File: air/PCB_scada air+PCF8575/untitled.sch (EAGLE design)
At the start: 122 parts, among them J1 C-GRID-03-70543, J10 C-GRID-03-70543, J11 C-GRID-03-70543, J12 C-GRID-03-70543, J13 C-GRID-03-70543, J14 C-GRID-03-70543, J15 C-GRID-03-70543, J16 C-GRID-03-70543, J17 C-GRID-03-70543, J18 C-GRID-03-70543, J19 C-GRID-03-70543, J2 C-GRID-03-70543, J20 C-GRID-03-70543, J21 C-GRID-03-70543, J3 C-GRID-03-70543, J4 C-GRID-03-70543, J5 C-GRID-03-70543, J6 C-GRID-03-70543, J7 C-GRID-03-70543, J8 C-GRID-03-70543, J9 C-GRID-03-70543, K1 351, Q1 MMBT2222, Q10 MMBT2222, Q11 MMBT2222, Q12 MMBT2222, Q13 MMBT2222, Q14 MMBT2222, Q15 MMBT2222, Q16 MMBT2222, Q17 MMBT2222, Q18 MMBT2222, Q19 MMBT2222, Q2 MMBT2222, Q20 MMBT2222, Q21 MMBT2222, Q22 S9013, Q3 MMBT2222, Q4 MMBT2222, Q5 MMBT2222, Q6 MMBT2222, Q7 MMBT2222, Q8 MMBT2222, Q9 MMBT2222, U1 ESP32-DEVKITC-32D, U2 PCF8575PW, U3 PCF8575PW, U4 PC817X2NIP0F, X1 C-GRID-02-70543, X2 C-GRID-02-70543, X3 MSTBA2, X4 C-GRID-03-70543, X5 C-GRID-02-70543, X6 C-GRID-02-70543, X7 MSTBA2, X8 MSTBA4, X9 MSTBA2

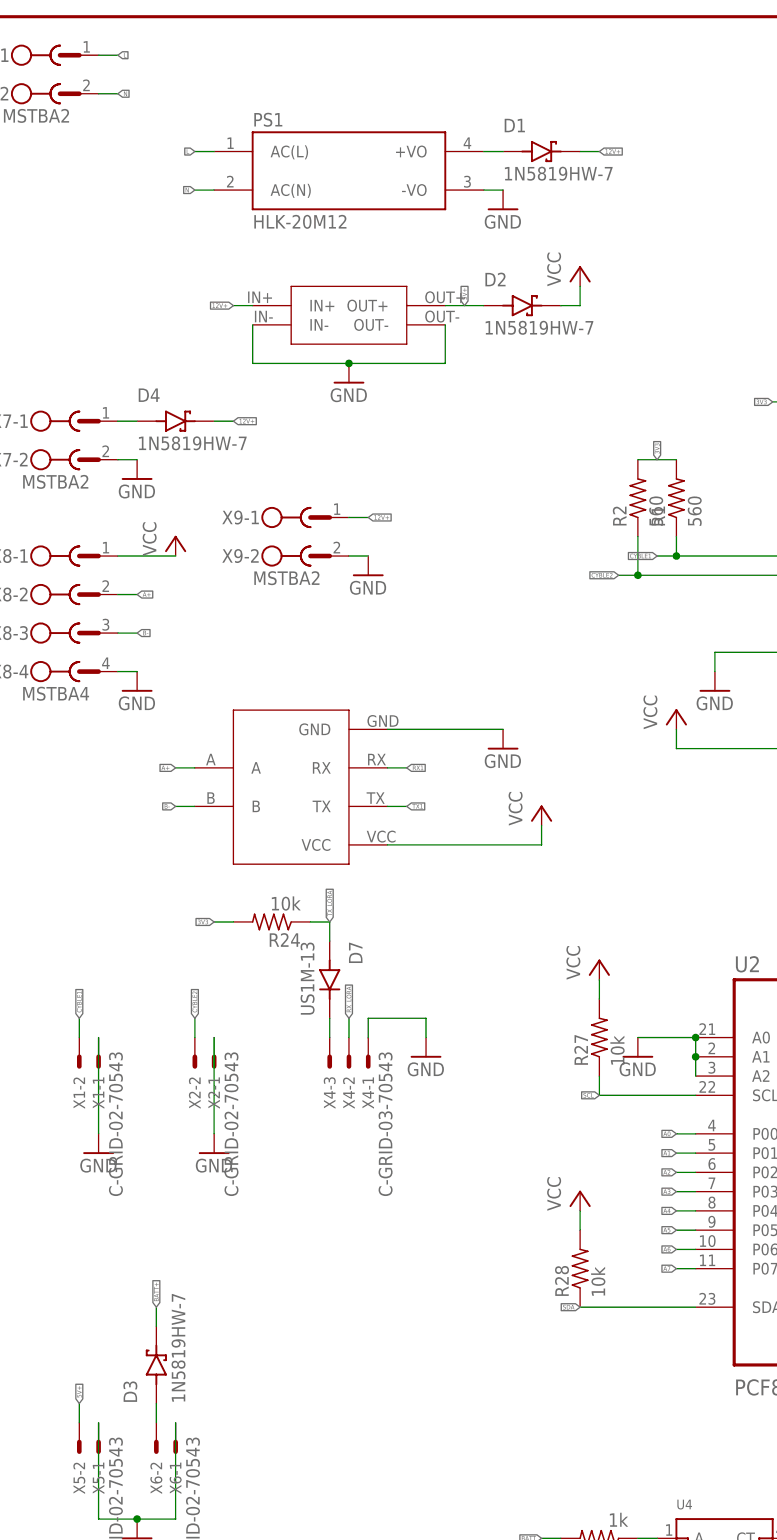
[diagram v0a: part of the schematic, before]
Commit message: revisi dioda schotky
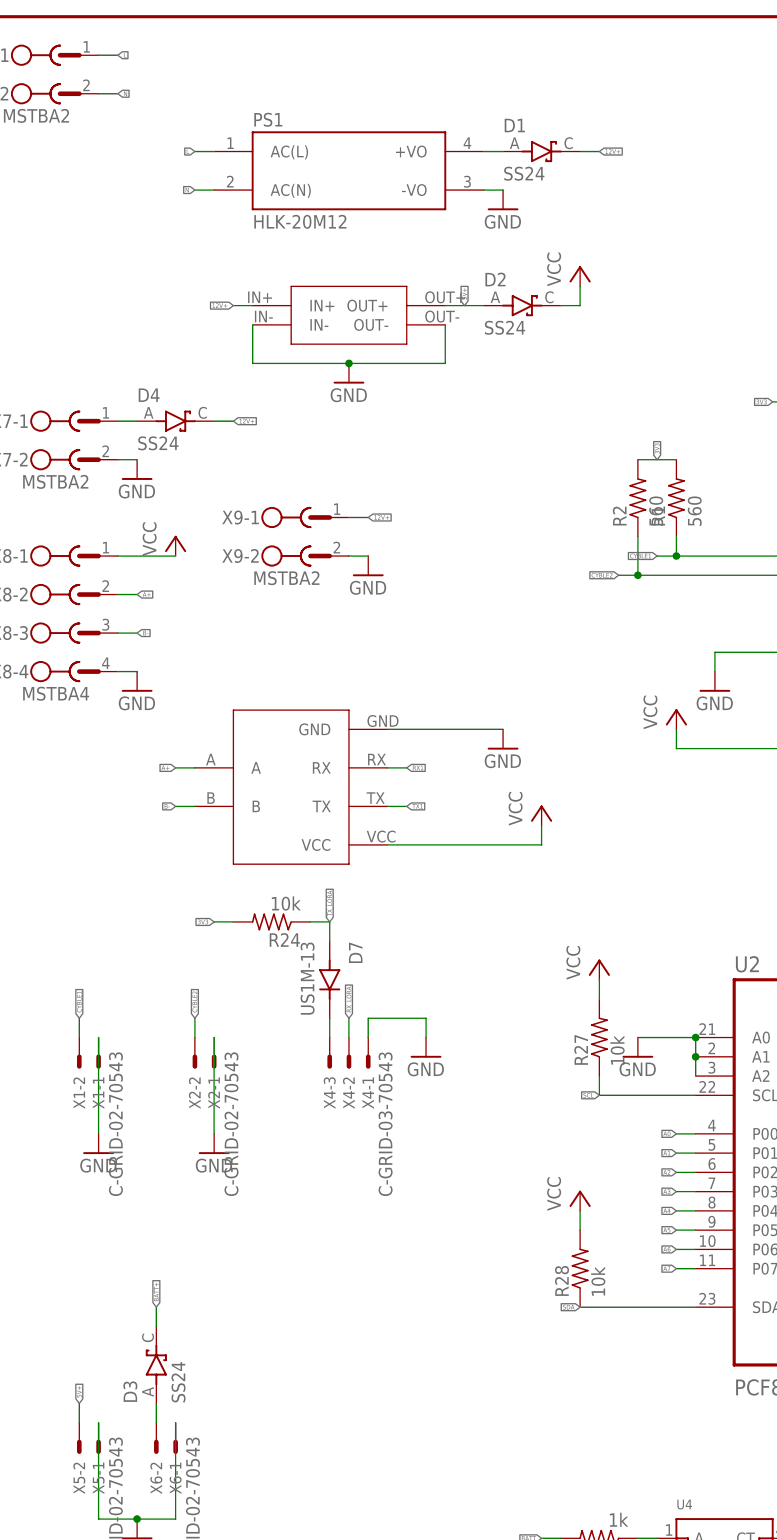
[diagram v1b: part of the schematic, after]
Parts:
- D1, D2, D3, D4: value 1N5819HW-7 -> SS24; device 1N5819HW-7:1N5819HW-7 -> SS24:SS24
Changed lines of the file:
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@@
 <part name="PS1" library="HLK-20M12" deviceset="HLK-20M12" device=""/>
 <part name="GND12" library="supply1" library_urn="urn:adsk.eagle:library:371" deviceset="GND" device=""/>
-<part name="D1" library="1N5819HW-7" deviceset="1N5819HW-7" device=""/>
+<part name="D1" library="SS24" deviceset="SS24" device=""/>
 <part name="MINI1" library="MINI560" deviceset="MINI560" device=""/>
 <part name="GND13" library="supply1" library_urn="urn:adsk.eagle:library:371" deviceset="GND" device=""/>
@@
 <part name="X4" library="con-molex" library_urn="urn:adsk.eagle:library:165" deviceset="C-GRID-03" device="-70543" package3d_urn="urn:adsk.eagle:package:8078684/1"/>
 <part name="GND20" library="supply1" library_urn="urn:adsk.eagle:library:371" deviceset="GND" device=""/>
-<part name="D2" library="1N5819HW-7" deviceset="1N5819HW-7" device=""/>
+<part name="D2" library="SS24" deviceset="SS24" device=""/>
 <part name="P+3" library="supply1" library_urn="urn:adsk.eagle:library:371" deviceset="VCC" device=""/>
 <part name="X5" library="con-molex" library_urn="urn:adsk.eagle:library:165" deviceset="C-GRID-02" device="-70543" package3d_urn="urn:adsk.eagle:package:8078681/1"/>
 <part name="X6" library="con-molex" library_urn="urn:adsk.eagle:library:165" deviceset="C-GRID-02" device="-70543" package3d_urn="urn:adsk.eagle:package:8078681/1"/>
 <part name="GND21" library="supply1" library_urn="urn:adsk.eagle:library:371" deviceset="GND" device=""/>
-<part name="D3" library="1N5819HW-7" deviceset="1N5819HW-7" device=""/>
+<part name="D3" library="SS24" deviceset="SS24" device=""/>
 <part name="Q1" library="MMBT2222_" deviceset="MMBT2222*" device=""/>
 <part name="Q2" library="MMBT2222_" deviceset="MMBT2222*" device=""/>
@@
 <part name="P+7" library="supply1" library_urn="urn:adsk.eagle:library:371" deviceset="VCC" device=""/>
 <part name="X7" library="con-phoenix-508" library_urn="urn:adsk.eagle:library:176" deviceset="MSTBA2" device="" package3d_urn="urn:adsk.eagle:package:9615/1"/>
-<part name="D4" library="1N5819HW-7" deviceset="1N5819HW-7" device=""/>
+<part name="D4" library="SS24" deviceset="SS24" device=""/>
 <part name="GND22" library="supply1" library_urn="urn:adsk.eagle:library:371" deviceset="GND" device=""/>
 <part name="TTL-RS1" library="TTL-RS485" deviceset="TTL-RS485" device=""/>

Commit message: revisi scada air
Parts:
- added JP1, JP2: (no value), adafruit:PINHD-1X3CB
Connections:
- new net GND1: JP1.1, JP1.2, JP1.3, JP2.1, JP2.2, JP2.3
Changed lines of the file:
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@@
 <layer number="48" name="Document" color="7" fill="1" visible="no" active="no"/>
 <layer number="49" name="Reference" color="7" fill="1" visible="no" active="no"/>
+<layer number="50" name="dxf" color="7" fill="1" visible="no" active="no"/>
 <layer number="51" name="tDocu" color="7" fill="1" visible="no" active="no"/>
 <layer number="52" name="bDocu" color="7" fill="1" visible="no" active="no"/>
+<layer number="53" name="tGND_GNDA" color="7" fill="9" visible="no" active="no"/>
+<layer number="54" name="bGND_GNDA" color="1" fill="9" visible="no" active="no"/>
+<layer number="56" name="wert" color="7" fill="1" visible="no" active="no"/>
+<layer number="57" name="tCAD" color="7" fill="1" visible="no" active="no"/>
+<layer number="59" name="tCarbon" color="7" fill="1" visible="no" active="no"/>
+<layer number="60" name="bCarbon" color="7" fill="1" visible="no" active="no"/>
 <layer number="88" name="SimResults" color="9" fill="1" visible="yes" active="yes"/>
 <layer number="89" name="SimProbes" color="9" fill="1" visible="yes" active="yes"/>
@@
 <layer number="97" name="Info" color="7" fill="1" visible="yes" active="yes"/>
 <layer number="98" name="Guide" color="6" fill="1" visible="yes" active="yes"/>
+<layer number="99" name="SpiceOrder" color="7" fill="1" visible="no" active="no"/>
+<layer number="100" name="Muster" color="7" fill="1" visible="no" active="no"/>
+<layer number="101" name="Patch_Top" color="12" fill="4" visible="no" active="yes"/>
+<layer number="102" name="Vscore" color="7" fill="1" visible="no" active="yes"/>
+<layer number="103" name="fp3" color="7" fill="1" visible="no" active="yes"/>
+<layer number="104" name="Name" color="7" fill="1" visible="no" active="yes"/>
+<layer number="105" name="Beschreib" color="9" fill="1" visible="no" active="yes"/>
+<layer number="106" name="BGA-Top" color="4" fill="1" visible="no" active="yes"/>
+<layer number="107" name="BD-Top" color="5" fill="1" visible="no" active="yes"/>
+<layer number="108" name="fp8" color="7" fill="1" visible="no" active="yes"/>
+<layer number="109" name="fp9" color="7" fill="1" visible="no" active="yes"/>
+<layer number="110" name="fp0" color="7" fill="1" visible="no" active="yes"/>
+<layer number="111" name="LPC17xx" color="7" fill="1" visible="no" active="yes"/>
+<layer number="112" name="tSilk" color="7" fill="1" visible="no" active="yes"/>
+<layer number="113" name="ReferenceLS" color="7" fill="1" visible="no" active="no"/>
+<layer number="116" name="Patch_BOT" color="9" fill="4" visible="no" active="yes"/>
+<layer number="118" name="Rect_Pads" color="7" fill="1" visible="no" active="no"/>
+<layer number="121" name="_tsilk" color="7" fill="1" visible="no" active="yes"/>
+<layer number="122" name="_bsilk" color="7" fill="1" visible="no" active="yes"/>
+<layer number="123" name="tTestmark" color="7" fill="1" visible="no" active="yes"/>
+<layer number="124" name="bTestmark" color="7" fill="1" visible="no" active="yes"/>
+<layer number="125" name="_tNames" color="7" fill="1" visible="no" active="yes"/>
+<layer number="126" name="_bNames" color="7" fill="1" visible="no" active="yes"/>
+<layer number="127" name="_tValues" color="7" fill="1" visible="no" active="yes"/>
+<layer number="128" name="_bValues" color="7" fill="1" visible="no" active="yes"/>
+<layer number="129" name="Mask" color="7" fill="1" visible="yes" active="yes"/>
+<layer number="131" name="tAdjust" color="7" fill="1" visible="no" active="yes"/>
+<layer number="132" name="bAdjust" color="7" fill="1" visible="no" active="yes"/>
+<layer number="144" name="Drill_legend" color="7" fill="1" visible="no" active="yes"/>
+<layer number="150" name="Notes" color="7" fill="1" visible="no" active="yes"/>
+<layer number="151" name="HeatSink" color="7" fill="1" visible="no" active="yes"/>
+<layer number="152" name="_bDocu" color="7" fill="1" visible="no" active="yes"/>
+<layer number="153" name="FabDoc1" color="6" fill="1" visible="no" active="no"/>
+<layer number="154" name="FabDoc2" color="2" fill="1" visible="no" active="no"/>
+<layer number="155" name="FabDoc3" color="7" fill="15" visible="no" active="no"/>
+<layer number="199" name="Contour" color="7" fill="1" visible="no" active="yes"/>
+<layer number="200" name="200bmp" color="1" fill="10" visible="no" active="yes"/>
+<layer number="201" name="201bmp" color="2" fill="1" visible="no" active="no"/>
+<layer number="202" name="202bmp" color="3" fill="1" visible="no" active="no"/>
+<layer number="203" name="203bmp" color="4" fill="10" visible="no" active="yes"/>
+<layer number="204" name="204bmp" color="5" fill="10" visible="no" active="yes"/>
+<layer number="205" name="205bmp" color="6" fill="10" visible="no" active="yes"/>
+<layer number="206" name="206bmp" color="7" fill="10" visible="no" active="yes"/>
+<layer number="207" name="207bmp" color="8" fill="10" visible="no" active="yes"/>
+<layer number="208" name="208bmp" color="9" fill="10" visible="no" active="yes"/>
+<layer number="209" name="209bmp" color="7" fill="1" visible="no" active="yes"/>
+<layer number="210" name="210bmp" color="7" fill="1" visible="no" active="yes"/>
+<layer number="211" name="211bmp" color="7" fill="1" visible="no" active="yes"/>
+<layer number="212" name="212bmp" color="7" fill="1" visible="no" active="yes"/>
+<layer number="213" name="213bmp" color="7" fill="1" visible="no" active="yes"/>
+<layer number="214" name="214bmp" color="7" fill="1" visible="no" active="yes"/>
+<layer number="215" name="215bmp" color="7" fill="1" visible="no" active="yes"/>
+<layer number="216" name="216bmp" color="7" fill="1" visible="no" active="yes"/>
+<layer number="217" name="217bmp" color="18" fill="1" visible="no" active="no"/>
+<layer number="218" name="218bmp" color="19" fill="1" visible="no" active="no"/>
+<layer number="219" name="219bmp" color="20" fill="1" visible="no" active="no"/>
+<layer number="220" name="220bmp" color="21" fill="1" visible="no" active="no"/>
+<layer number="221" name="221bmp" color="22" fill="1" visible="no" active="no"/>
+<layer number="222" name="222bmp" color="23" fill="1" visible="no" active="no"/>
+<layer number="223" name="223bmp" color="24" fill="1" visible="no" active="no"/>
+<layer number="224" name="224bmp" color="25" fill="1" visible="no" active="no"/>
+<layer number="225" name="225bmp" color="7" fill="1" visible="yes" active="yes"/>
+<layer number="226" name="226bmp" color="7" fill="1" visible="yes" active="yes"/>
+<layer number="227" name="227bmp" color="7" fill="1" visible="yes" active="yes"/>
+<layer number="228" name="228bmp" color="7" fill="1" visible="yes" active="yes"/>
+<layer number="229" name="229bmp" color="7" fill="1" visible="yes" active="yes"/>
+<layer number="230" name="230bmp" color="7" fill="1" visible="yes" active="yes"/>
+<layer number="231" name="Eagle3D_PG1" color="7" fill="1" visible="no" active="no"/>
+<layer number="232" name="Eagle3D_PG2" color="7" fill="1" visible="no" active="no"/>
+<layer number="233" name="Eagle3D_PG3" color="7" fill="1" visible="no" active="no"/>
+<layer number="248" name="Housing" color="7" fill="1" visible="no" active="yes"/>
+<layer number="249" name="Edge" color="7" fill="1" visible="no" active="yes"/>
+<layer number="250" name="Descript" color="7" fill="1" visible="no" active="no"/>
+<layer number="251" name="SMDround" color="7" fill="1" visible="no" active="no"/>
+<layer number="254" name="cooling" color="7" fill="1" visible="no" active="yes"/>
+<layer number="255" name="routoute" color="7" fill="1" visible="yes" active="yes"/>
 </layers>
 <schematic xreflabel="%F%N/%S.%C%R" xrefpart="/%S.%C%R">
@@
 <part name="GND40" library="supply1" library_urn="urn:adsk.eagle:library:371" deviceset="GND" device=""/>
 <part name="P+5" library="supply1" library_urn="urn:adsk.eagle:library:371" deviceset="VCC" device=""/>
+<part name="JP1" library="adafruit" library_urn="urn:adsk.eagle:library:420" deviceset="PINHD-1X3" device="CB" package3d_urn="urn:adsk.eagle:package:6240706/1"/>
+<part name="JP2" library="adafruit" library_urn="urn:adsk.eagle:library:420" deviceset="PINHD-1X3" device="CB" package3d_urn="urn:adsk.eagle:package:6240706/1"/>
 </parts>
 <sheets>
@@
 <instance part="P+5" gate="VCC" x="149.86" y="218.44" smashed="yes">
 <attribute name="VALUE" x="147.32" y="215.9" size="1.778" layer="96" rot="R90"/>
+</instance>
+<instance part="JP1" gate="A" x="5.08" y="378.46" smashed="yes" rot="R180">
+<attribute name="NAME" x="11.43" y="372.745" size="1.778" layer="95" rot="R180"/>
+<attribute name="VALUE" x="11.43" y="386.08" size="1.778" layer="96" rot="R180"/>
+</instance>
+<instance part="JP2" gate="A" x="5.08" y="363.22" smashed="yes" rot="R180">
+<attribute name="NAME" x="11.43" y="357.505" size="1.778" layer="95" rot="R180"/>
+<attribute name="VALUE" x="11.43" y="370.84" size="1.778" layer="96" rot="R180"/>
 </instance>
 </instances>
@@
 </segment>
 </net>
+<net name="GND1" class="0">
+<segment>
+<pinref part="JP1" gate="A" pin="3"/>
+<pinref part="JP1" gate="A" pin="2"/>
+<wire x1="7.62" y1="381" x2="7.62" y2="378.46" width="0.1524" layer="91"/>
+<pinref part="JP1" gate="A" pin="1"/>
+<wire x1="7.62" y1="378.46" x2="7.62" y2="375.92" width="0.1524" layer="91"/>
+<junction x="7.62" y="378.46"/>
+<label x="7.62" y="375.92" size="0.6096" layer="95" xref="yes"/>
+</segment>
+<segment>
+<pinref part="JP2" gate="A" pin="3"/>
+<pinref part="JP2" gate="A" pin="2"/>
+<wire x1="7.62" y1="365.76" x2="7.62" y2="363.22" width="0.1524" layer="91"/>
+<pinref part="JP2" gate="A" pin="1"/>
+<wire x1="7.62" y1="363.22" x2="7.62" y2="360.68" width="0.1524" layer="91"/>
+<junction x="7.62" y="363.22"/>
+<label x="7.62" y="360.68" size="0.6096" layer="95" xref="yes"/>
+</segment>
+</net>
